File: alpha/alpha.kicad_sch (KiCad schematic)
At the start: 32 parts, among them J1 Conn_01x02, J10 Conn_01x03, J2 Conn_01x02, J3 Conn_01x03, J4 Conn_01x03, J5 Conn_01x03, J6 Conn_01x03, J7 Conn_01x03, J8 Conn_01x03, J9 Conn_01x03, M1 Motor_AC_3_phase, M2 Motor_AC_3_phase, M3 Motor_AC_3_phase, M4 Motor_AC_3_phase, U1 Holybro Pixhawk 6X, U10 Radiomaster Bandit BR3 ELRS, U12 5V, 5A step down converter, U13 Holybro Digital Air Speed Sen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, U14 Holybro I2C board, U15 Crazyflie Flow v2, U2 Holybro PM08D Power Module, U3 Holybro Tekko32 F4 Metal 4in1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, U4 iFlight Anti Spark Filter, U5 RFD868x, U6 Holybro M9N GPS, U7 3.3V, 0.6A step down converter, U8 Walksnail Avatar HD Pro Kit, U9 12V, 4.5A step down converter

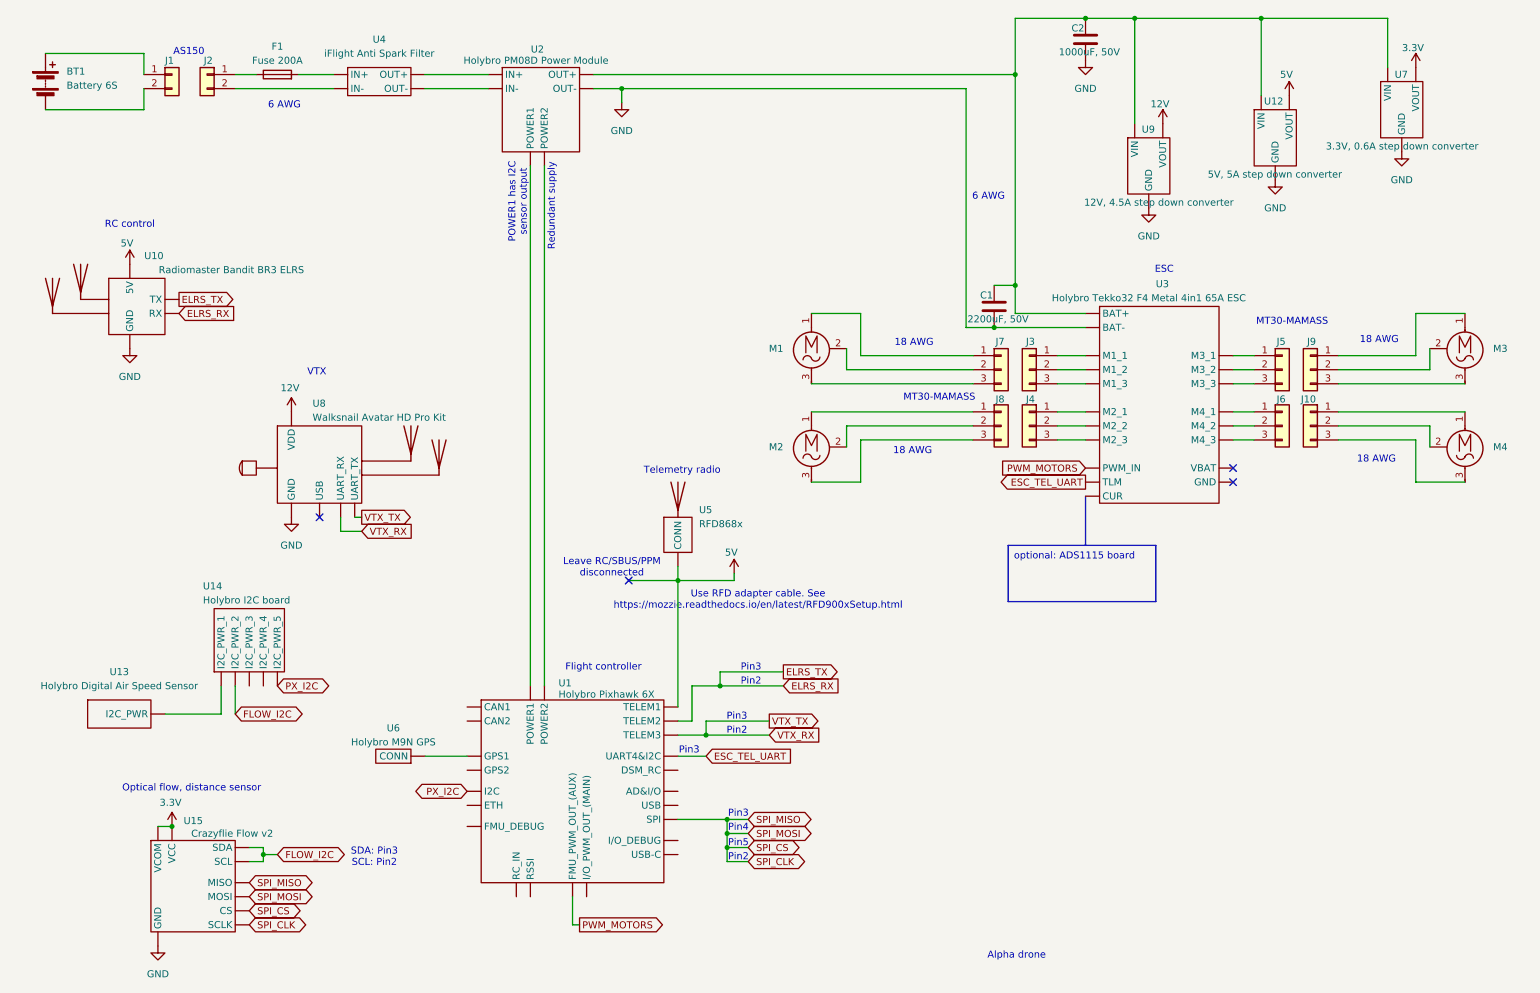
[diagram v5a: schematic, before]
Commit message: Add cam servo
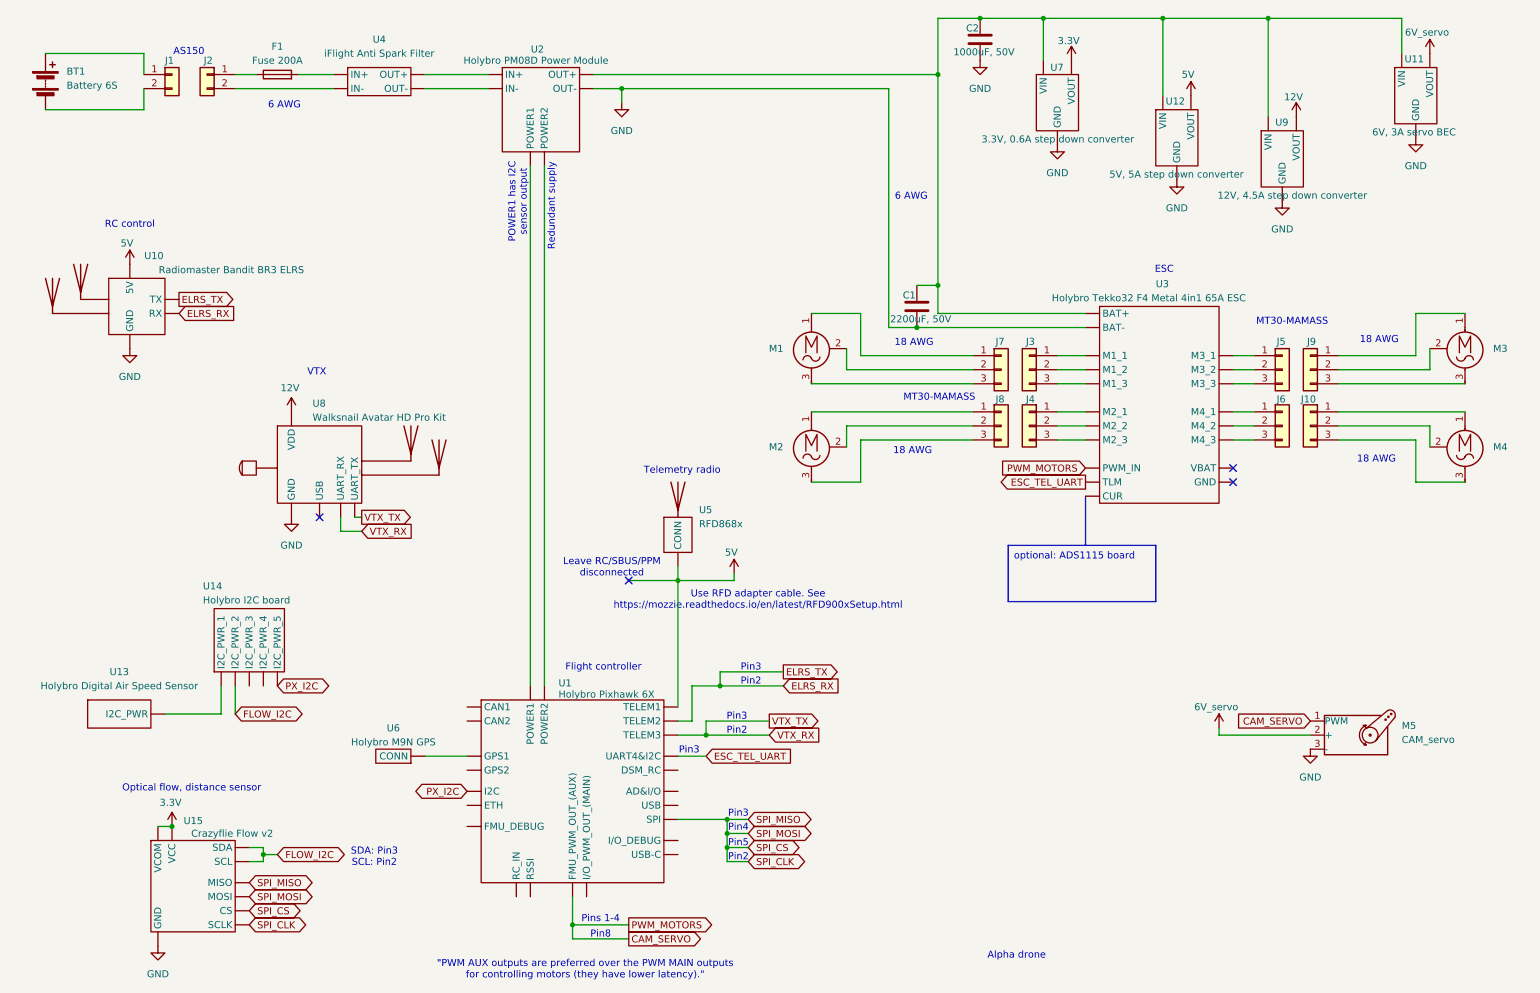
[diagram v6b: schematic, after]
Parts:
- added M5: CAM_servo, symbol Motor:Motor_Servo
- added U11: 6V, 3A servo BEC, symbol DC_DC_Converters:DC/DC_Converter
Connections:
- net GND: now also M5.3 (-), U11. (VOUT)
- net at U4. (OUT-): now also F1.2; no longer U2. (POWER2)
- removed net PWM_MOTORS: U1. (USB-C), U3. (VBAT)
- new net: C1.1, C2.1, U11. (VOUT), U12. (VOUT), U2. (POWER2), U3. (VBAT), U7. (VOUT), U9. (VOUT)
- new net: U1. (USB-C), U2. (POWER2) (x2)
- new net: U2. (POWER2), U4. (OUT-) (x2)
- new net 6V_servo: M5.2 (+), U11. (VOUT)
- new net CAM_SERVO: M5.1 (PWM), U1. (USB-C), U3. (VBAT)
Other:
- note added: ""PWM AUX outputs are preferred over the PWM MAIN outputs for controlling motors (they have lower latency).""
- note added: "Pin8"
- note added: "Pins 1-4"
- moved on the sheet: C1, C2, U12, U7, U9

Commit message: update
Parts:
- removed U5: RFD868x, symbol RF_Modules:RFD868x-EU_868Mhz_Long_Range
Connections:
- net 5V: no longer U1. (USB-C)
- net at U4. (OUT-): now also F1.2; no longer U2. (POWER2)
- new net: C1.1, C2.1, U11. (VOUT), U12. (VOUT), U2. (POWER2), U3. (VBAT), U7. (VOUT), U9. (VOUT)
- new net: U1. (USB-C), U2. (POWER2) (x2)
- new net: U2. (POWER2), U4. (OUT-) (x2)
- no-connect marks 4 -> 3
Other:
- note removed: "Leave RC/SBUS/PPM disconnected"
- note removed: "Telemetry radio"
- note removed: "Use RFD adapter cable. See https://mozzie.readthedocs.io/en/latest/RFD900xSetup.html"
